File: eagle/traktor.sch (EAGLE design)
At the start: 20 parts

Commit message: secound version
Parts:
- added 5V1, A3, A7, D1, D6, GND_1: I_O_PIN, traktor:I_O_PIN
- added LED1: (no value), led:LED5MM
- added R6: (no value), resistor:R-EU_R0805
- R3, R4, R5: value 6K8 -> (none); device resistor:R-EU_R0603 -> resistor:R-EU_R0805
- U$4, U$6: value I_O_PIN -> BUTTON; device traktor:I_O_PIN -> traktor:BUTTON
- renumbered D9 to D13, U$5 to 5V, U$7 to GND_
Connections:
- new net GND1: GND_1.P$1, LED1.C, R5.2
- new net N$20: 5V1.P$1, R4.2, U$6.A
- new net N$21: LED1.A, R6.1
- new net N$22: D1.P$1, R6.2
- new net N$9: A7.P$1, U$1.A7
- net 5V: now also 5V.P$1; no longer R3.2, R4.2, R5.2
- net N$16: now also U$1.D13; no longer U$1.D9
- net N$17: now also D6.P$1, U$1.D6; no longer R4.1, U$1.D8, U$4.P$1
- net N$18: now also A3.P$1, R3.2, U$4.B; no longer 5V.P$1, U$1.D7
- net N$19: now also R4.1, U$4.A, U$6.B; no longer U$1.D6, U$6.P$1
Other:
- moved on the sheet: R3, R4, R5

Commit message: 5V Instead Of D13
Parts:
- renumbered D13 to 5V_1
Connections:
- removed net N$16: 5V_1.P$1, U$1.D13
- net 5V: now also 5V_1.P$1
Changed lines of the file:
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@@
 <part name="GND" library="traktor" deviceset="I_O_PIN" device=""/>
 <part name="VIN" library="traktor" deviceset="I_O_PIN" device=""/>
-<part name="D13" library="traktor" deviceset="I_O_PIN" device=""/>
+<part name="5V_1" library="traktor" deviceset="I_O_PIN" device=""/>
 <part name="A2" library="traktor" deviceset="I_O_PIN" device=""/>
 <part name="D6" library="traktor" deviceset="I_O_PIN" device=""/>
@@
 <instance part="GND" gate="G$1" x="-83.82" y="73.66" rot="R90"/>
 <instance part="VIN" gate="G$1" x="-88.9" y="73.66" rot="R90"/>
-<instance part="D13" gate="G$1" x="-53.34" y="73.66" rot="R90"/>
+<instance part="5V_1" gate="G$1" x="-53.34" y="73.66" rot="R90"/>
 <instance part="A2" gate="G$1" x="-68.58" y="73.66" rot="R90"/>
 <instance part="D6" gate="G$1" x="127" y="12.7"/>
@@
 <wire x1="-33.02" y1="-2.54" x2="-15.24" y2="-2.54" width="0.1524" layer="91"/>
 <pinref part="SDA" gate="G$1" pin="P$1"/>
-<wire x1="-58.42" y1="73.66" x2="-58.42" y2="50.8" width="0.1524" layer="91"/>
-<wire x1="-58.42" y1="50.8" x2="-40.64" y2="50.8" width="0.1524" layer="91"/>
-<wire x1="-40.64" y1="50.8" x2="-40.64" y2="-7.62" width="0.1524" layer="91"/>
+<wire x1="-58.42" y1="73.66" x2="-58.42" y2="45.72" width="0.1524" layer="91"/>
+<wire x1="-58.42" y1="45.72" x2="-40.64" y2="45.72" width="0.1524" layer="91"/>
+<wire x1="-40.64" y1="45.72" x2="-40.64" y2="-7.62" width="0.1524" layer="91"/>
 <junction x="-40.64" y="-7.62"/>
 </segment>
@@
 <wire x1="-38.1" y1="-2.54" x2="-45.72" y2="-2.54" width="0.1524" layer="91"/>
 <wire x1="-45.72" y1="-2.54" x2="-53.34" y2="-2.54" width="0.1524" layer="91"/>
-<wire x1="-45.72" y1="-2.54" x2="-45.72" y2="45.72" width="0.1524" layer="91"/>
+<wire x1="-45.72" y1="-2.54" x2="-45.72" y2="40.64" width="0.1524" layer="91"/>
 <pinref part="SCL" gate="G$1" pin="P$1"/>
-<wire x1="-45.72" y1="45.72" x2="-63.5" y2="45.72" width="0.1524" layer="91"/>
-<wire x1="-63.5" y1="45.72" x2="-63.5" y2="73.66" width="0.1524" layer="91"/>
+<wire x1="-45.72" y1="40.64" x2="-63.5" y2="40.64" width="0.1524" layer="91"/>
+<wire x1="-63.5" y1="40.64" x2="-63.5" y2="73.66" width="0.1524" layer="91"/>
 <junction x="-45.72" y="-2.54"/>
 </segment>
@@
 <wire x1="-15.24" y1="12.7" x2="-78.74" y2="12.7" width="0.1524" layer="91"/>
 <wire x1="-78.74" y1="12.7" x2="-78.74" y2="73.66" width="0.1524" layer="91"/>
-</segment>
-</net>
-<net name="N$16" class="0">
-<segment>
-<pinref part="D13" gate="G$1" pin="P$1"/>
-<wire x1="-53.34" y1="55.88" x2="-53.34" y2="73.66" width="0.1524" layer="91"/>
-<wire x1="-53.34" y1="55.88" x2="-35.56" y2="55.88" width="0.1524" layer="91"/>
-<wire x1="-35.56" y1="55.88" x2="-35.56" y2="33.02" width="0.1524" layer="91"/>
-<pinref part="U$1" gate="G$1" pin="D13"/>
-<wire x1="-35.56" y1="33.02" x2="-15.24" y2="33.02" width="0.1524" layer="91"/>
 </segment>
 </net>
@@
 <wire x1="121.92" y1="7.62" x2="121.92" y2="50.8" width="0.1524" layer="91"/>
 <junction x="121.92" y="50.8"/>
-</segment>
-</net>
+<wire x1="-30.48" y1="50.8" x2="-53.34" y2="50.8" width="0.1524" layer="91"/>
+<pinref part="5V_1" gate="G$1" pin="P$1"/>
+<wire x1="-53.34" y1="50.8" x2="-53.34" y2="73.66" width="0.1524" layer="91"/>
+<junction x="-30.48" y="50.8"/>
+</segment>
+</net>

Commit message: added 7805
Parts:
- added C1: 330 nF, resistor:C-EUC0805
- added C2: 100nF, resistor:C-EUC0805
- added D2: 1N4004, diode:1N4004
- added DC1: R-78C5.0-1.0, dc-dc-converter:R-78C5.0-1.0
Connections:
- new net VIN: D2.A, VIN.P$1
- net 5V: now also C2.1, DC1.VOUT
- net GND: now also C1.2, C2.2, DC1.GND, U$2.D0, U$2.D1, U$2.D2, U$2.D3
- net N$13: now also C1.1, D2.C, DC1.VIN; no longer U$1.VIN, VIN.P$1
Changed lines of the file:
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@@
 <?xml version="1.0" encoding="utf-8"?>
 <!DOCTYPE eagle SYSTEM "eagle.dtd">
-<eagle version="8.0.0">
+<eagle version="9.0.1">
 <drawing>
 <settings>
 <setting alwaysvectorfont="no"/>
+<setting keepoldvectorfont="yes"/>
 <setting verticaltext="up"/>
 </settings>
@@
 <part name="R6" library="resistor" deviceset="R-EU_" device="R0805"/>
 <part name="LED1" library="led" deviceset="LED" device="5MM"/>
+<part name="DC1" library="dc-dc-converter" library_urn="urn:adsk.eagle:library:208" deviceset="R-78C*-1.0" device="" package3d_urn="urn:adsk.eagle:package:12318/1" technology="5.0"/>
+<part name="C1" library="resistor" library_urn="urn:adsk.eagle:library:348" deviceset="C-EU" device="C0805" package3d_urn="urn:adsk.eagle:package:26137/1" value="330 nF"/>
+<part name="C2" library="resistor" library_urn="urn:adsk.eagle:library:348" deviceset="C-EU" device="C0805" package3d_urn="urn:adsk.eagle:package:26137/1" value="100nF"/>
+<part name="D2" library="diode" library_urn="urn:adsk.eagle:library:210" deviceset="1N4004" device="" package3d_urn="urn:adsk.eagle:package:43336/1"/>
 </parts>
 <sheets>
@@
 <instance part="R6" gate="G$1" x="177.8" y="33.02" rot="R90"/>
 <instance part="LED1" gate="G$1" x="177.8" y="22.86"/>
+<instance part="DC1" gate="G$1" x="-66.04" y="-48.26"/>
+<instance part="C1" gate="G$1" x="-88.9" y="-50.8"/>
+<instance part="C2" gate="G$1" x="-43.18" y="-50.8"/>
+<instance part="D2" gate="1" x="-88.9" y="-40.64" rot="R270"/>
 </instances>
 <busses>
@@
 <pinref part="U$2" gate="G$1" pin="RW"/>
 <wire x1="114.3" y1="45.72" x2="106.68" y2="45.72" width="0.1524" layer="91"/>
-<wire x1="106.68" y1="45.72" x2="50.8" y2="45.72" width="0.1524" layer="91"/>
+<wire x1="106.68" y1="45.72" x2="86.36" y2="45.72" width="0.1524" layer="91"/>
+<wire x1="86.36" y1="45.72" x2="50.8" y2="45.72" width="0.1524" layer="91"/>
 <wire x1="106.68" y1="55.88" x2="106.68" y2="45.72" width="0.1524" layer="91"/>
 <junction x="106.68" y="45.72"/>
@@
 <wire x1="127" y1="45.72" x2="127" y2="17.78" width="0.1524" layer="91"/>
 <junction x="127" y="45.72"/>
+<wire x1="-25.4" y1="-33.02" x2="-25.4" y2="-58.42" width="0.1524" layer="91"/>
+<pinref part="DC1" gate="G$1" pin="GND"/>
+<wire x1="-25.4" y1="-58.42" x2="-43.18" y2="-58.42" width="0.1524" layer="91"/>
+<wire x1="-43.18" y1="-58.42" x2="-66.04" y2="-58.42" width="0.1524" layer="91"/>
+<wire x1="-66.04" y1="-58.42" x2="-66.04" y2="-55.88" width="0.1524" layer="91"/>
+<label x="-88.9" y="-55.88" size="1.778" layer="95"/>
+<label x="-88.9" y="-55.88" size="1.778" layer="95"/>
+<pinref part="C1" gate="G$1" pin="2"/>
+<wire x1="-66.04" y1="-58.42" x2="-88.9" y2="-58.42" width="0.1524" layer="91"/>
+<wire x1="-88.9" y1="-58.42" x2="-88.9" y2="-55.88" width="0.1524" layer="91"/>
+<junction x="-66.04" y="-58.42"/>
+<pinref part="C2" gate="G$1" pin="2"/>
+<wire x1="-43.18" y1="-55.88" x2="-43.18" y2="-58.42" width="0.1524" layer="91"/>
+<junction x="-43.18" y="-58.42"/>
+<pinref part="U$2" gate="G$1" pin="D3"/>
+<pinref part="U$2" gate="G$1" pin="D2"/>
+<wire x1="81.28" y1="55.88" x2="86.36" y2="55.88" width="0.1524" layer="91"/>
+<pinref part="U$2" gate="G$1" pin="D1"/>
+<wire x1="86.36" y1="55.88" x2="91.44" y2="55.88" width="0.1524" layer="91"/>
+<junction x="86.36" y="55.88"/>
+<pinref part="U$2" gate="G$1" pin="D0"/>
+<wire x1="91.44" y1="55.88" x2="96.52" y2="55.88" width="0.1524" layer="91"/>
+<junction x="91.44" y="55.88"/>
+<wire x1="86.36" y1="55.88" x2="86.36" y2="45.72" width="0.1524" layer="91"/>
+<junction x="86.36" y="45.72"/>
 </segment>
 </net>
@@
 <net name="N$13" class="0">
 <segment>
-<pinref part="U$1" gate="G$1" pin="VIN"/>
-<pinref part="VIN" gate="G$1" pin="P$1"/>
-<wire x1="-15.24" y1="-38.1" x2="-88.9" y2="-38.1" width="0.1524" layer="91"/>
-<wire x1="-88.9" y1="-38.1" x2="-88.9" y2="73.66" width="0.1524" layer="91"/>
+<wire x1="-88.9" y1="-48.26" x2="-88.9" y2="-43.18" width="0.1524" layer="91"/>
+<pinref part="DC1" gate="G$1" pin="VIN"/>
+<wire x1="-88.9" y1="-48.26" x2="-78.74" y2="-48.26" width="0.1524" layer="91"/>
+<pinref part="C1" gate="G$1" pin="1"/>
+<junction x="-88.9" y="-48.26"/>
+<pinref part="D2" gate="1" pin="C"/>
 </segment>
 </net>
@@
 <wire x1="-53.34" y1="50.8" x2="-53.34" y2="73.66" width="0.1524" layer="91"/>
 <junction x="-30.48" y="50.8"/>
+<pinref part="DC1" gate="G$1" pin="VOUT"/>
+<wire x1="-53.34" y1="-48.26" x2="-43.18" y2="-48.26" width="0.1524" layer="91"/>
+<wire x1="-43.18" y1="-48.26" x2="-30.48" y2="-48.26" width="0.1524" layer="91"/>
+<wire x1="-30.48" y1="-48.26" x2="-30.48" y2="-22.86" width="0.1524" layer="91"/>
+<junction x="-30.48" y="-22.86"/>
+<pinref part="C2" gate="G$1" pin="1"/>
+<junction x="-43.18" y="-48.26"/>
 </segment>
 </net>
@@
 </segment>
 </net>
+<net name="VIN" class="0">
+<segment>
+<pinref part="VIN" gate="G$1" pin="P$1"/>
+<wire x1="-88.9" y1="-38.1" x2="-88.9" y2="73.66" width="0.1524" layer="91"/>
+<pinref part="D2" gate="1" pin="A"/>
+</segment>
+</net>
 </nets>
 </sheet>
@@
 </schematic>
 </drawing>
+<compatibility>
+<note version="8.2" severity="warning">
+Since Version 8.2, EAGLE supports online libraries. The ids
+of those online libraries will not be understood (or retained)
+with this version.
+</note>
+<note version="8.3" severity="warning">
+Since Version 8.3, EAGLE supports URNs for individual library
+assets (packages, symbols, and devices). The URNs of those assets
+will not be understood (or retained) with this version.
+</note>
+<note version="8.3" severity="warning">
+Since Version 8.3, EAGLE supports the association of 3D packages
+with devices in libraries, schematics, and board files. Those 3D
+packages will not be understood (or retained) with this version.
+</note>
+</compatibility>
 </eagle>

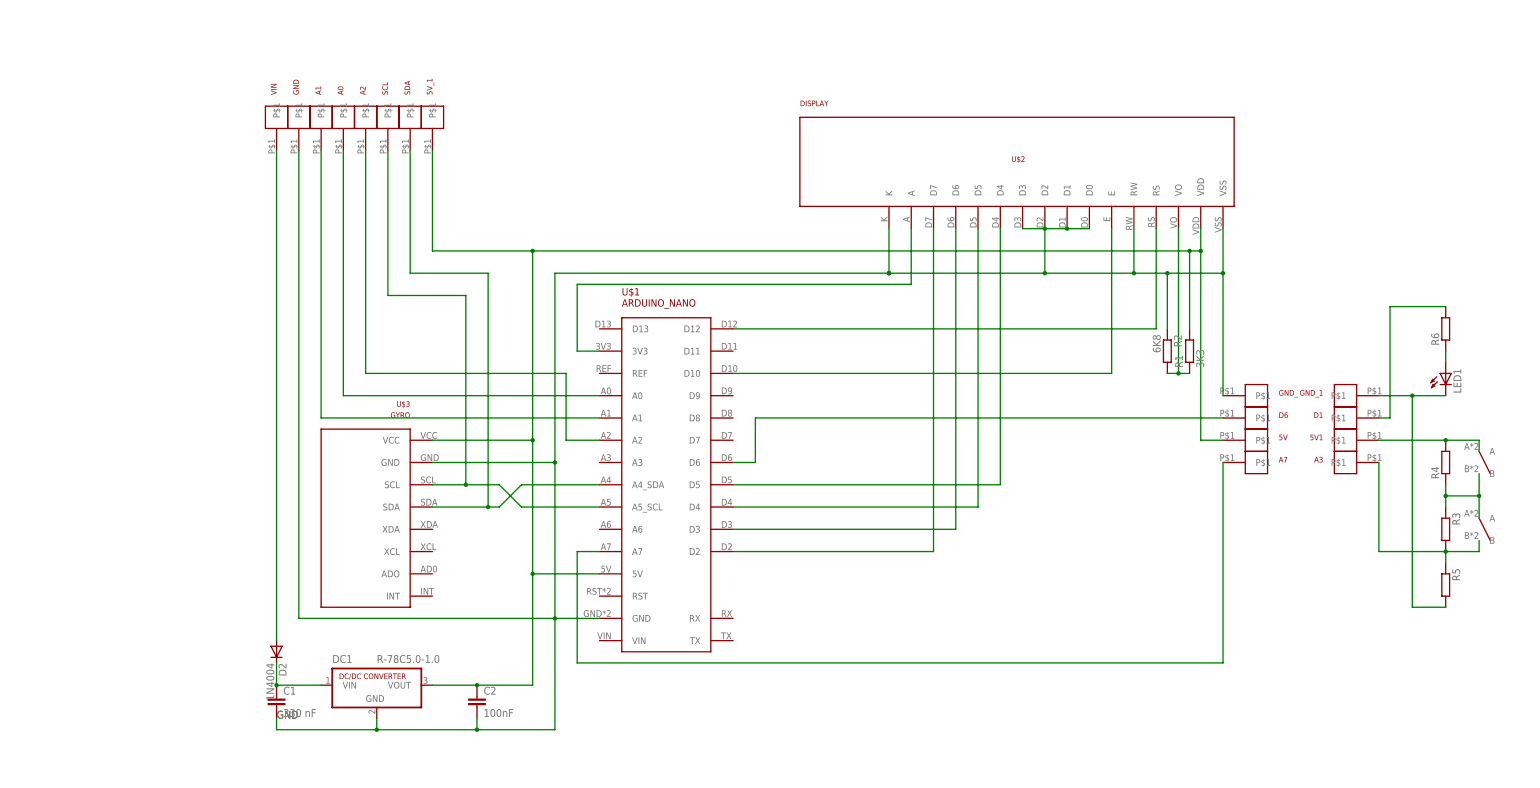
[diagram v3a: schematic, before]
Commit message: changes for external MPU and LED bar - PCB redesigned to two layer one
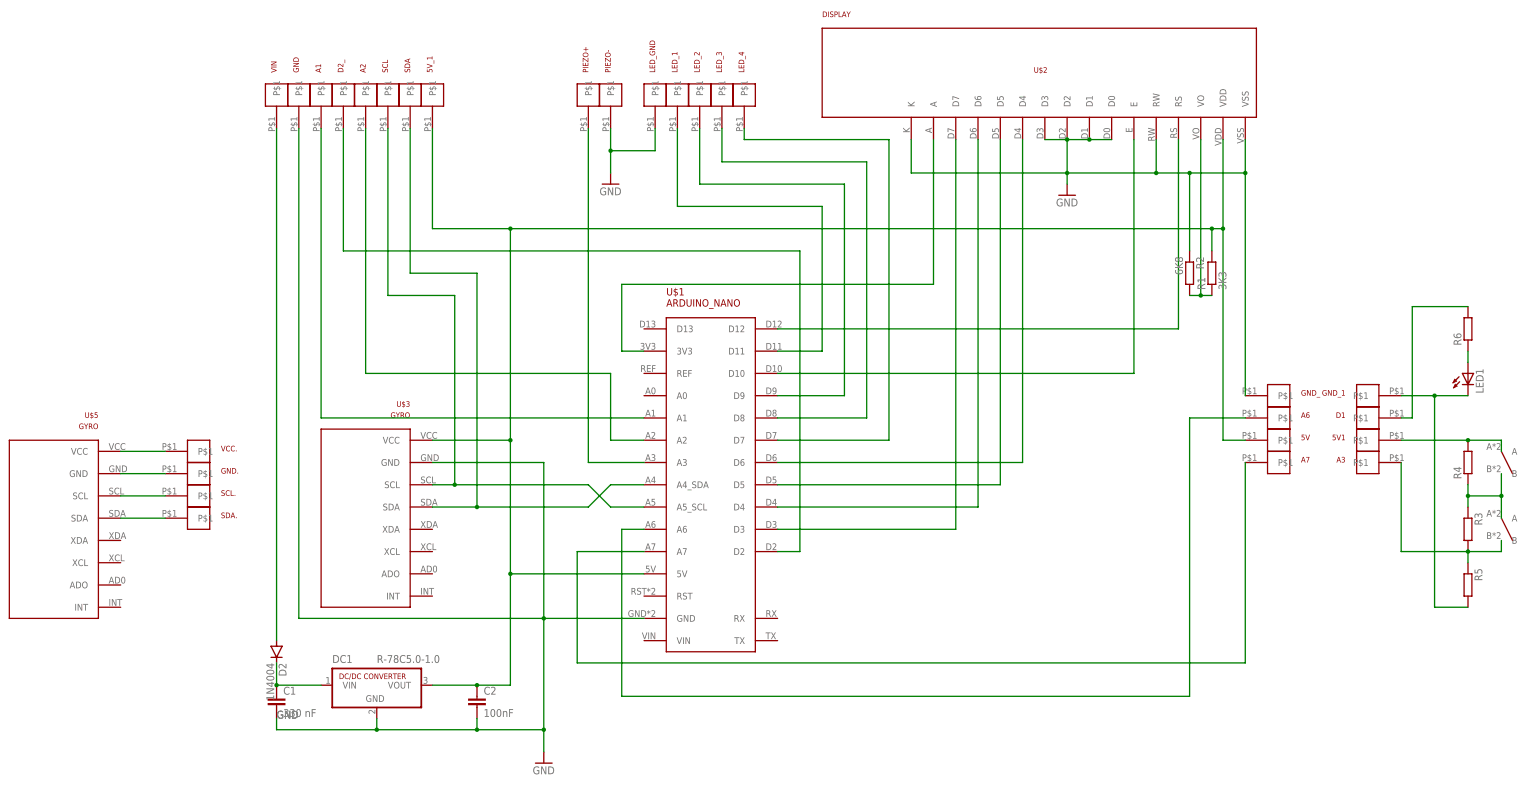
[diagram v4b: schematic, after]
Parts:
- removed A0, D6: I_O_PIN, traktor:I_O_PIN
- added A6, D2_, GND., LED_1, LED_2, LED_3, LED_4, LED_GND, PIEZO+, PIEZO-, SCL., SDA., VCC.: I_O_PIN, traktor:I_O_PIN
- added U$5: GYRO, traktor:GYRO
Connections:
- new net N$16: PIEZO+.P$1, U$1.A3
- new net N$27: LED_1.P$1, U$1.D11
- new net N$28: LED_2.P$1, U$1.D9
- new net N$29: LED_3.P$1, U$1.D8
- new net N$30: LED_4.P$1, U$1.D7
- new net N$31: U$5.VCC, VCC..P$1
- new net N$32: GND..P$1, U$5.GND
- new net N$33: SCL..P$1, U$5.SCL
- new net N$34: SDA..P$1, U$5.SDA
- net GND: now also LED_GND.P$1, PIEZO-.P$1
- net N$14: now also D2_.P$1, U$1.D2; no longer A0.P$1, U$1.A0
- net N$17: now also A6.P$1, U$1.A6; no longer D6.P$1, U$1.D6
- net N$3: now also U$1.D3; no longer U$1.D2
- net N$4: now also U$1.D4; no longer U$1.D3
- net N$5: now also U$1.D5; no longer U$1.D4
- net N$6: now also U$1.D6; no longer U$1.D5
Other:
- moved on the sheet: 5V, 5V1, 5V_1, A1, A2, A3, A7, D1, GND, GND_, GND_1, LED1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

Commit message: version 2023-05-04
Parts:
- R3, R5: value (none) -> 10k
- R4: value (none) -> 4k7
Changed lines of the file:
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@@
 <part name="A3" library="traktor" deviceset="I_O_PIN" device=""/>
 <part name="GND_1" library="traktor" deviceset="I_O_PIN" device=""/>
-<part name="R3" library="resistor" deviceset="R-EU_" device="R0805"/>
-<part name="R4" library="resistor" deviceset="R-EU_" device="R0805"/>
-<part name="R5" library="resistor" deviceset="R-EU_" device="R0805"/>
+<part name="R3" library="resistor" deviceset="R-EU_" device="R0805" value="10k"/>
+<part name="R4" library="resistor" deviceset="R-EU_" device="R0805" value="4k7"/>
+<part name="R5" library="resistor" deviceset="R-EU_" device="R0805" value="10k"/>
 <part name="R6" library="resistor" deviceset="R-EU_" device="R0805"/>
 <part name="LED1" library="led" deviceset="LED" device="5MM"/>
@@
 <attribute name="NAME" x="144.78" y="17.78" size="1.27" layer="94"/>
 </instance>
-<instance part="U$4" gate="G$1" x="190.5" y="-12.7" smashed="yes" rot="R270"/>
-<instance part="U$6" gate="G$1" x="190.5" y="2.54" smashed="yes" rot="R270"/>
+<instance part="U$4" gate="G$1" x="193.04" y="-12.7" smashed="yes" rot="R270"/>
+<instance part="U$6" gate="G$1" x="193.04" y="2.54" smashed="yes" rot="R270"/>
 <instance part="D1" gate="G$1" x="167.64" y="12.7" smashed="yes" rot="MR0">
 <attribute name="NAME" x="154.94" y="12.7" size="1.27" layer="94" rot="MR0"/>
@@
 </instance>
 <instance part="R3" gate="G$1" x="182.88" y="-12.7" smashed="yes" rot="R270">
-<attribute name="NAME" x="184.3786" y="-8.89" size="1.778" layer="95" rot="R270"/>
+<attribute name="NAME" x="184.3786" y="-11.43" size="1.778" layer="95" rot="R270"/>
 <attribute name="VALUE" x="179.578" y="-8.89" size="1.778" layer="96" rot="R270"/>
 </instance>
 <instance part="R4" gate="G$1" x="182.88" y="2.54" smashed="yes" rot="R90">
-<attribute name="NAME" x="181.3814" y="-1.27" size="1.778" layer="95" rot="R90"/>
-<attribute name="VALUE" x="186.182" y="-1.27" size="1.778" layer="96" rot="R90"/>
+<attribute name="NAME" x="184.3786" y="3.81" size="1.778" layer="95" rot="R270"/>
+<attribute name="VALUE" x="179.578" y="6.35" size="1.778" layer="96" rot="R270"/>
 </instance>
 <instance part="R5" gate="G$1" x="182.88" y="-25.4" smashed="yes" rot="R270">
-<attribute name="NAME" x="184.3786" y="-21.59" size="1.778" layer="95" rot="R270"/>
+<attribute name="NAME" x="184.3786" y="-24.13" size="1.778" layer="95" rot="R270"/>
 <attribute name="VALUE" x="179.578" y="-21.59" size="1.778" layer="96" rot="R270"/>
 </instance>
@@
 <pinref part="U$4" gate="G$1" pin="A"/>
 <wire x1="182.88" y1="-5.08" x2="182.88" y2="-2.54" width="0.1524" layer="91"/>
-<wire x1="190.5" y1="0" x2="190.5" y2="-5.08" width="0.1524" layer="91"/>
-<wire x1="190.5" y1="-5.08" x2="190.5" y2="-10.16" width="0.1524" layer="91"/>
-<wire x1="182.88" y1="-5.08" x2="190.5" y2="-5.08" width="0.1524" layer="91"/>
+<wire x1="193.04" y1="0" x2="193.04" y2="-5.08" width="0.1524" layer="91"/>
+<wire x1="193.04" y1="-5.08" x2="193.04" y2="-10.16" width="0.1524" layer="91"/>
+<wire x1="182.88" y1="-5.08" x2="193.04" y2="-5.08" width="0.1524" layer="91"/>
 <junction x="182.88" y="-5.08"/>
-<junction x="190.5" y="-5.08"/>
+<junction x="193.04" y="-5.08"/>
 </segment>
 </net>
@@
 <pinref part="R3" gate="G$1" pin="2"/>
 <pinref part="U$4" gate="G$1" pin="B"/>
-<wire x1="190.5" y1="-17.78" x2="190.5" y2="-15.24" width="0.1524" layer="91"/>
-<wire x1="190.5" y1="-17.78" x2="182.88" y2="-17.78" width="0.1524" layer="91"/>
+<wire x1="193.04" y1="-17.78" x2="193.04" y2="-15.24" width="0.1524" layer="91"/>
+<wire x1="193.04" y1="-17.78" x2="182.88" y2="-17.78" width="0.1524" layer="91"/>
 <junction x="182.88" y="-17.78"/>
 <pinref part="R5" gate="G$1" pin="1"/>
@@
 <pinref part="R4" gate="G$1" pin="2"/>
 <pinref part="U$6" gate="G$1" pin="A"/>
-<wire x1="190.5" y1="5.08" x2="190.5" y2="7.62" width="0.1524" layer="91"/>
-<wire x1="190.5" y1="7.62" x2="182.88" y2="7.62" width="0.1524" layer="91"/>
+<wire x1="193.04" y1="5.08" x2="193.04" y2="7.62" width="0.1524" layer="91"/>
+<wire x1="193.04" y1="7.62" x2="182.88" y2="7.62" width="0.1524" layer="91"/>
 <junction x="182.88" y="7.62"/>
 <pinref part="5V1" gate="G$1" pin="P$1"/>
